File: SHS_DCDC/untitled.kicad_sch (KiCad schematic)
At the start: 32 parts, among them J1 PJ-059A, Q1 BSS84, Q14 PMV100XPEAR, Q15 2N7002-dk_Transistors-FETs-MO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, Q16 PMV100XPEAR, Q22 2N7002-dk_Transistors-FETs-MO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, Q23 2N7002-dk_Transistors-FETs-MO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, U1 RT8299-WDFN10L

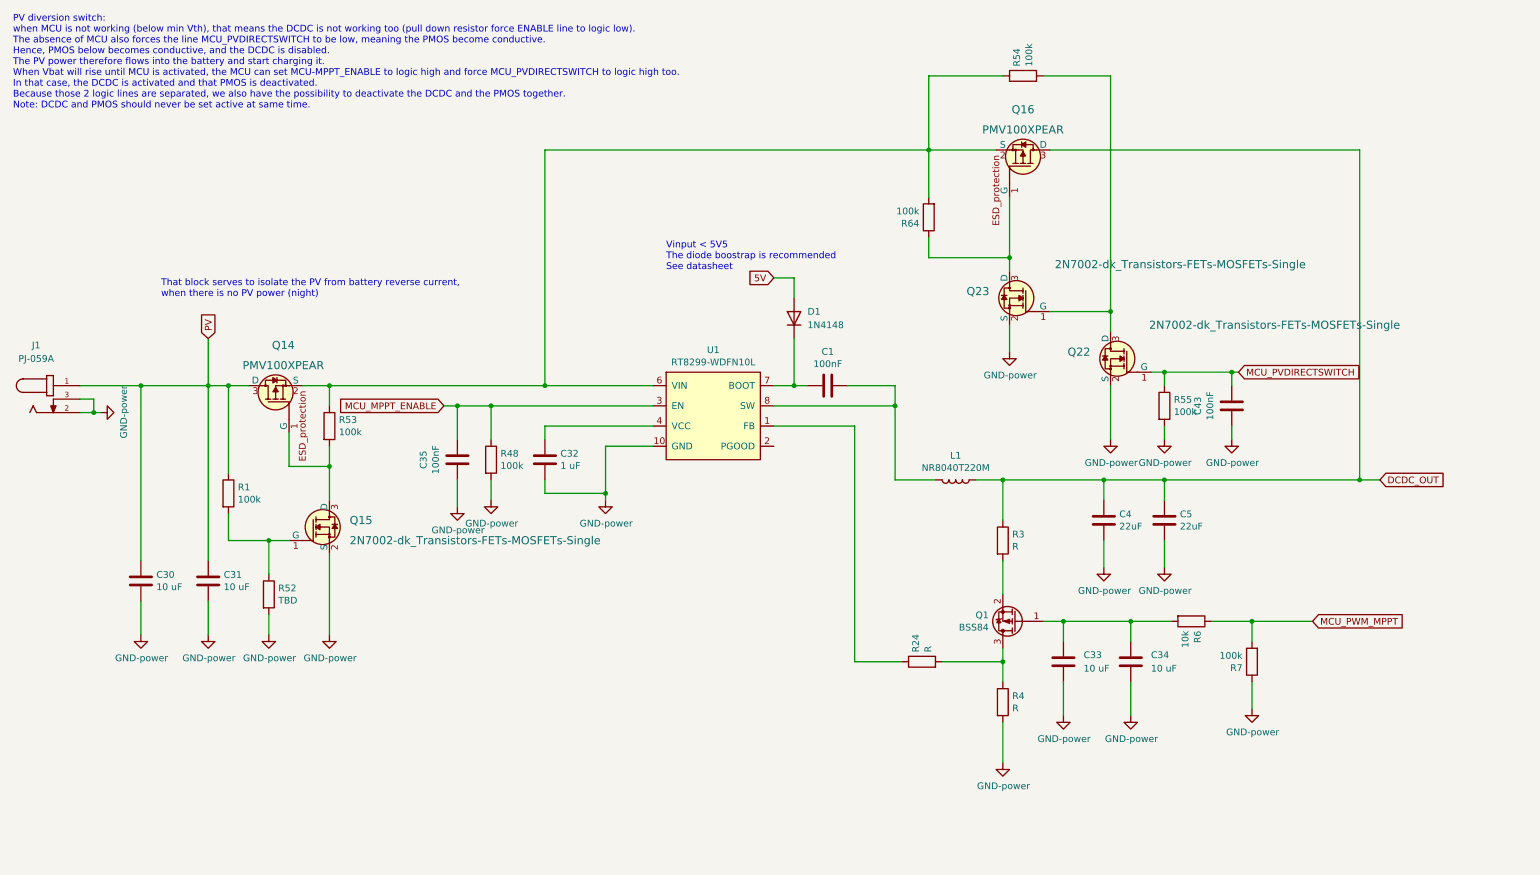
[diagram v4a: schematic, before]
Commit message: Commit before reannotation
Plan to test the reannotation feature.
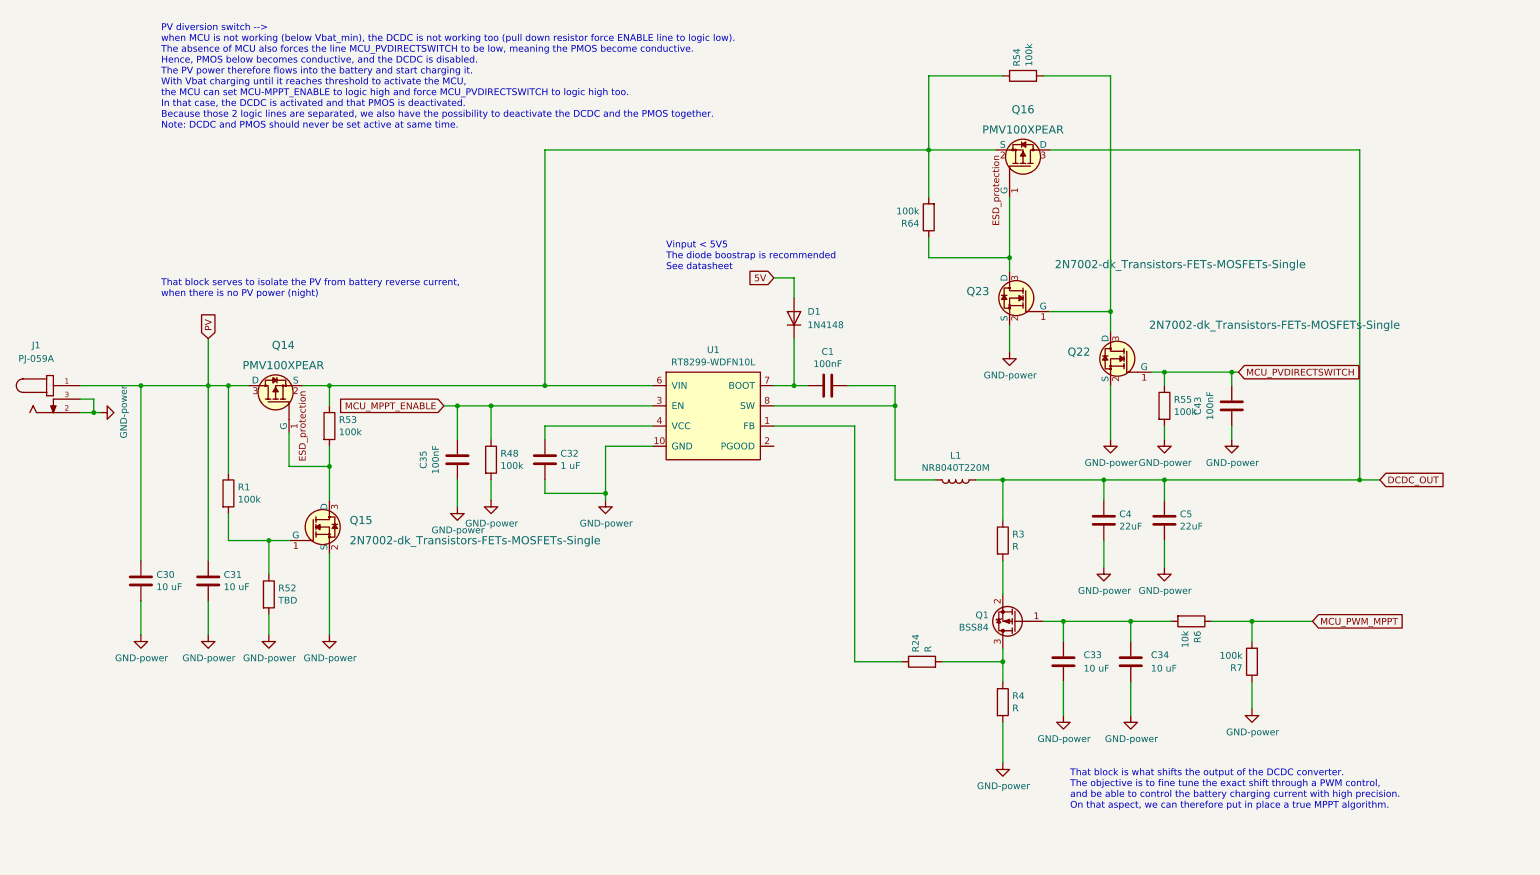
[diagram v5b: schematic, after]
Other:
- note added: "PV diversion switch --> when MCU is not working (below Vbat_min), the DCDC is not working too (pull down resistor force ENABLE line to logic low). The absence of MCU also forces the line MCU_PVDIRECTSWITCH to be low, meaning the PMOS become conductive. Hence, PMOS below becomes conductive, and the DCDC is disabled. The PV power therefore flows into the battery and start charging it. With Vbat cha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"
- note added: "That block is what shifts the output of the DCDC converter. The objective is to fine tune the exact shift through a PWM control, and be able to control the battery charging current with high precision. On that aspect, we can therefore put in place a true MPPT algorithm."
- note removed: "PV diversion switch: when MCU is not working (below min Vth), that means the DCDC is not working too (pull down resistor force ENABLE line to logic low). The absence of MCU also forces the line MCU_PVDIRECTSWITCH to be low, meaning the PMOS become conductive. Hence, PMOS below becomes conductive, and the DCDC is disabled. The PV power therefore flows into the battery and start charging it. When V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"
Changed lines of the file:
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@@
     (stroke (width 0) (type default) (color 0 0 0 0))
   )
-  (text "PV diversion switch:\nwhen MCU is not working (below min Vth), that means the DCDC is not working too (pull down resistor force ENABLE line to logic low).\nThe absence of MCU also forces the line MCU_PVDIRECTSWITCH to be low, meaning the PMOS become conductive.\nHence, PMOS below becomes conductive, and the DCDC is disabled.\nThe PV power therefore flows into the battery and start charging it.\nWhen Vbat will rise until MCU is activated, the MCU can set MCU-MPPT_ENABLE to logic high and force MCU_PVDIRECTSWITCH to logic high too.\nIn that case, the DCDC is activated and that PMOS is deactivated. \nBecause those 2 logic lines are separated, we also have the possibility to deactivate the DCDC and the PMOS together. \nNote: DCDC and PMOS should never be set active at same time."
-    (at 13.97 31.75 0)
+  (text "That block is what shifts the output of the DCDC converter.\nThe objective is to fine tune the exact shift through a PWM control,\nand be able to control the battery charging current with high precision.\nOn that aspect, we can therefore put in place a true MPPT algorithm."
+    (at 213.36 163.83 0)
     (effects (font (size 1.27 1.27)) (justify left bottom))
   )
+  (text "PV diversion switch -->\nwhen MCU is not working (below Vbat_min), the DCDC is not working too (pull down resistor force ENABLE line to logic low).\nThe absence of MCU also forces the line MCU_PVDIRECTSWITCH to be low, meaning the PMOS become conductive.\nHence, PMOS below becomes conductive, and the DCDC is disabled.\nThe PV power therefore flows into the battery and start charging it.\nWith Vbat charging until it reaches threshold to activate the MCU, \nthe MCU can set MCU-MPPT_ENABLE to logic high and force MCU_PVDIRECTSWITCH to logic high too.\nIn that case, the DCDC is activated and that PMOS is deactivated. \nBecause those 2 logic lines are separated, we also have the possibility to deactivate the DCDC and the PMOS together. \nNote: DCDC and PMOS should never be set active at same time."
+    (at 41.91 35.56 0)
+    (effects (font (size 1.27 1.27)) (justify left bottom))
+  )

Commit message: Testpoints
All the tests points have been placed
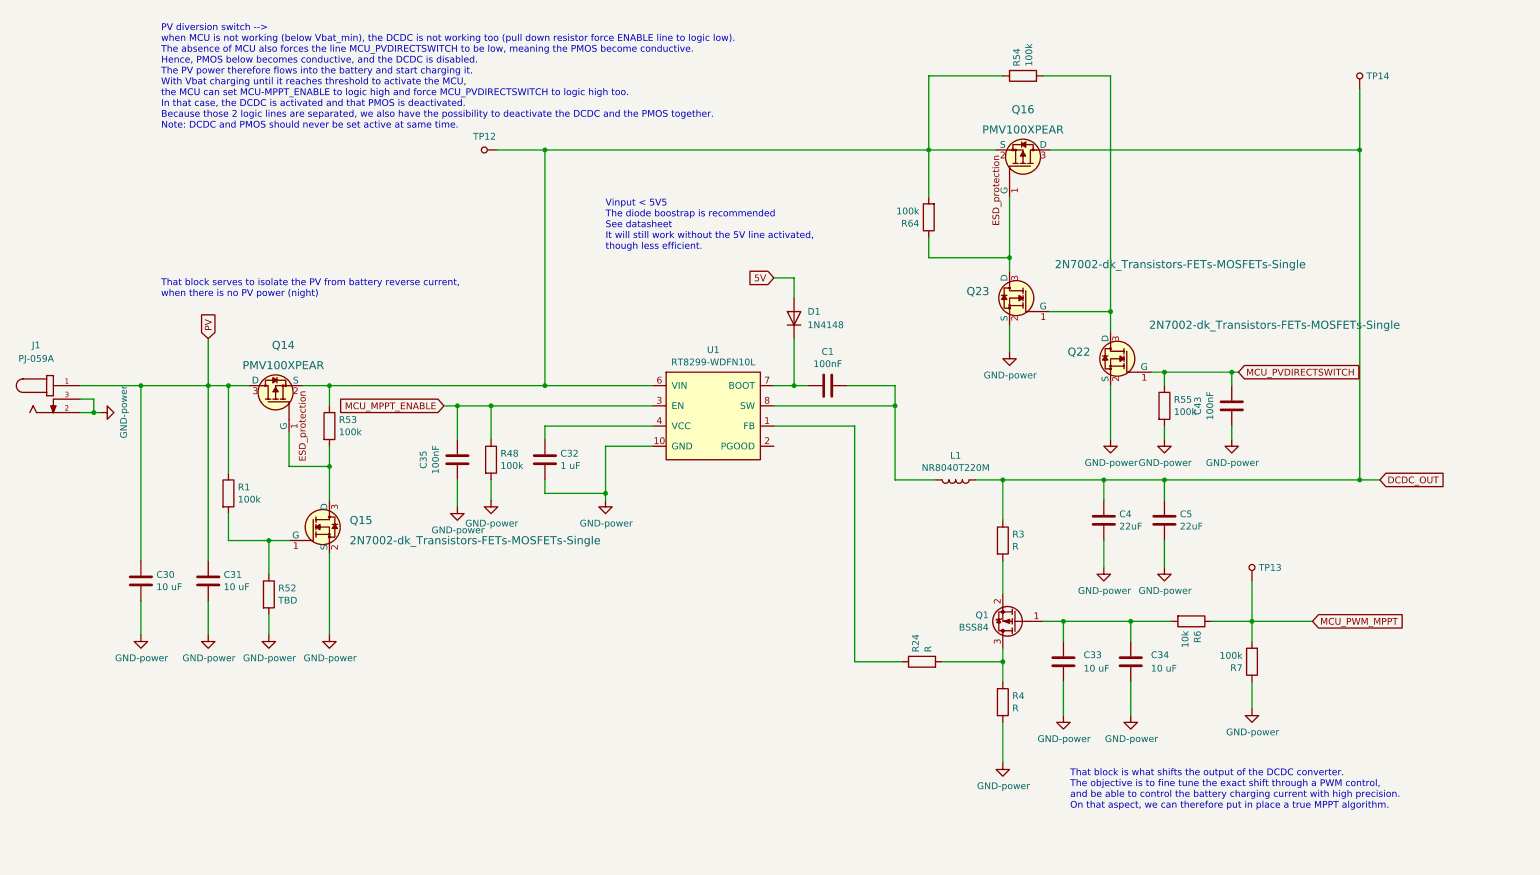
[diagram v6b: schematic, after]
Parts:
- added TP12, TP13, TP14: 5029, digikey-footprints:PC_Test_Point_Mini_3.8x2.03mm, symbol dk_Test-Points:5029
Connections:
- net DCDC_OUT: now also TP14.1
- net MCU_PWM_MPPT: now also TP13.1
- net at Q14.2 (S), Q16.2 (S), R53.1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: now also TP12.1
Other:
- note added: "Vinput < 5V5 The diode boostrap is recommended See datasheet It will still work without the 5V line activated, though less efficient."
- note removed: "Vinput < 5V5 The diode boostrap is recommended See datasheet"
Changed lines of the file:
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@@
 (kicad_sch (version 20211123) (generator eeschema)
   (paper "A4")
+  (junction (at 267.97 39.37) (diameter 0) (color 0 0 0 0)
+  )
   (junction (at 125.73 104.14) (diameter 0) (color 0 0 0 0)
   )
@@
   (junction (at 200.66 101.6) (diameter 0) (color 0 0 0 0)
   )
+  (junction (at 114.3 39.37) (diameter 0) (color 0 0 0 0)
+  )
   (junction (at 73.66 83.82) (diameter 0) (color 0 0 0 0)
   )
@@
     (stroke (width 0) (type default) (color 0 0 0 0))
   )
+  (wire (pts (xy 267.97 27.94) (xy 267.97 39.37))
+    (stroke (width 0) (type default) (color 0 0 0 0))
+  )
   (wire (pts (xy 243.84 81.28) (xy 243.84 83.82))
     (stroke (width 0) (type default) (color 0 0 0 0))
@@
     (stroke (width 0) (type default) (color 0 0 0 0))
   )
+  (wire (pts (xy 105.41 39.37) (xy 114.3 39.37))
+    (stroke (width 0) (type default) (color 0 0 0 0))
+  )
   (wire (pts (xy 38.1 116.84) (xy 38.1 83.82))
     (stroke (width 0) (type default) (color 0 0 0 0))
@@
   )
   (wire (pts (xy 201.93 72.39) (xy 201.93 77.47))
+    (stroke (width 0) (type default) (color 0 0 0 0))
+  )
+  (wire (pts (xy 247.65 120.65) (xy 247.65 128.27))
     (stroke (width 0) (type default) (color 0 0 0 0))
   )
@@
     (effects (font (size 1.27 1.27)) (justify left bottom))
   )
-  (text "Vinput < 5V5\nThe diode boostrap is recommended\nSee datasheet"
-    (at 137.16 62.23 0)
+  (text "Vinput < 5V5\nThe diode boostrap is recommended\nSee datasheet\nIt will still work without the 5V line activated,\nthough less efficient."
+    (at 125.73 58.42 0)
     (effects (font (size 1.27 1.27)) (justify left bottom))
   )
@@
     (pin "2")
   )
+  (symbol (lib_id "dk_Test-Points:5029") (at 247.65 118.11 180) (unit 1)
+    (in_bom yes) (on_board yes) (fields_autoplaced)
+    (property "Reference" "TP13" (id 0) (at 248.92 118.148 0)
+      (effects (font (size 1.27 1.27)) (justify right))
+    )
+    (property "Value" "5029" (id 1) (at 247.65 115.57 0)
+      (effects (font (size 1.27 1.27)) hide)
+    )
+    (property "Footprint" "digikey-footprints:PC_Test_Point_Mini_3.8x2.03mm" (id 2) (at 242.57 123.19 0)
+      (effects (font (size 1.524 1.524)) (justify left) hide)
+    )
+    (property "Datasheet" "http://www.keyelco.com/product-pdf.cfm?p=1358" (id 3) (at 242.57 125.73 0)
+      (effects (font (size 1.524 1.524)) (justify left) hide)
+    )
+    (property "Digi-Key_PN" "36-5029CT-ND" (id 4) (at 242.57 128.27 0)
+      (effects (font (size 1.524 1.524)) (justify left) hide)
+    )
+    (property "MPN" "5029" (id 5) (at 242.57 130.81 0)
+      (effects (font (size 1.524 1.524)) (justify left) hide)
+    )
+    (property "Category" "Test and Measurement" (id 6) (at 242.57 133.35 0)
+      (effects (font (size 1.524 1.524)) (justify left) hide)
+    )
+    (property "Family" "Test Points" (id 7) (at 242.57 135.89 0)
+      (effects (font (size 1.524 1.524)) (justify left) hide)
+    )
+    (property "DK_Datasheet_Link" "http://www.keyelco.com/product-pdf.cfm?p=1358" (id 8) (at 242.57 138.43 0)
+      (effects (font (size 1.524 1.524)) (justify left) hide)
+    )
+    (property "DK_Detail_Page" "/product-detail/en/keystone-electronics/5029/36-5029CT-ND/5980631" (id 9) (at 242.57 140.97 0)
+      (effects (font (size 1.524 1.524)) (justify left) hide)
+    )
+    (property "Description" "PC TEST POINT MINIATURE" (id 10) (at 242.57 143.51 0)
+      (effects (font (size 1.524 1.524)) (justify left) hide)
+    )
+    (property "Manufacturer" "Keystone Electronics" (id 11) (at 242.57 146.05 0)
+      (effects (font (size 1.524 1.524)) (justify left) hide)
+    )
+    (property "Status" "Active" (id 12) (at 242.57 148.59 0)
+      (effects (font (size 1.524 1.524)) (justify left) hide)
+    )
+    (pin "1")
+  )
   (symbol (lib_id "SHS_DCDC:R-Device") (at 186.69 52.07 180) (unit 1)
     (in_bom yes) (on_board yes)
@@
     (pin "3")
   )
+  (symbol (lib_id "dk_Test-Points:5029") (at 267.97 25.4 180) (unit 1)
+    (in_bom yes) (on_board yes) (fields_autoplaced)
+    (property "Reference" "TP14" (id 0) (at 269.24 25.438 0)
+      (effects (font (size 1.27 1.27)) (justify right))
+    )
+    (property "Value" "5029" (id 1) (at 267.97 22.86 0)
+      (effects (font (size 1.27 1.27)) hide)
+    )
+    (property "Footprint" "digikey-footprints:PC_Test_Point_Mini_3.8x2.03mm" (id 2) (at 262.89 30.48 0)
+      (effects (font (size 1.524 1.524)) (justify left) hide)
+    )
+    (property "Datasheet" "http://www.keyelco.com/product-pdf.cfm?p=1358" (id 3) (at 262.89 33.02 0)
+      (effects (font (size 1.524 1.524)) (justify left) hide)
+    )
+    (property "Digi-Key_PN" "36-5029CT-ND" (id 4) (at 262.89 35.56 0)
+      (effects (font (size 1.524 1.524)) (justify left) hide)
+    )
+    (property "MPN" "5029" (id 5) (at 262.89 38.1 0)
+      (effects (font (size 1.524 1.524)) (justify left) hide)
+    )
+    (property "Category" "Test and Measurement" (id 6) (at 262.89 40.64 0)
+      (effects (font (size 1.524 1.524)) (justify left) hide)
+    )
+    (property "Family" "Test Points" (id 7) (at 262.89 43.18 0)
+      (effects (font (size 1.524 1.524)) (justify left) hide)
+    )
+    (property "DK_Datasheet_Link" "http://www.keyelco.com/product-pdf.cfm?p=1358" (id 8) (at 262.89 45.72 0)
+      (effects (font (size 1.524 1.524)) (justify left) hide)
+    )
+    (property "DK_Detail_Page" "/product-detail/en/keystone-electronics/5029/36-5029CT-ND/5980631" (id 9) (at 262.89 48.26 0)
+      (effects (font (size 1.524 1.524)) (justify left) hide)
+    )
+    (property "Description" "PC TEST POINT MINIATURE" (id 10) (at 262.89 50.8 0)
+      (effects (font (size 1.524 1.524)) (justify left) hide)
+    )
+    (property "Manufacturer" "Keystone Electronics" (id 11) (at 262.89 53.34 0)
+      (effects (font (size 1.524 1.524)) (justify left) hide)
+    )
+    (property "Status" "Active" (id 12) (at 262.89 55.88 0)
+      (effects (font (size 1.524 1.524)) (justify left) hide)
+    )
+    (pin "1")
+  )
   (symbol (lib_id "SHS_DCDC:PMV100XPEAR") (at 63.5 83.82 90) (unit 1)
     (in_bom yes) (on_board yes)
@@
     (pin "2")
   )
+  (symbol (lib_id "dk_Test-Points:5029") (at 102.87 39.37 270) (unit 1)
+    (in_bom yes) (on_board yes) (fields_autoplaced)
+    (property "Reference" "TP12" (id 0) (at 102.9081 36.83 90))
+    (property "Value" "5029" (id 1) (at 100.33 39.37 0)
+      (effects (font (size 1.27 1.27)) hide)
+    )
+    (property "Footprint" "digikey-footprints:PC_Test_Point_Mini_3.8x2.03mm" (id 2) (at 107.95 44.45 0)
+      (effects (font (size 1.524 1.524)) (justify left) hide)
+    )
+    (property "Datasheet" "http://www.keyelco.com/product-pdf.cfm?p=1358" (id 3) (at 110.49 44.45 0)
+      (effects (font (size 1.524 1.524)) (justify left) hide)
+    )
+    (property "Digi-Key_PN" "36-5029CT-ND" (id 4) (at 113.03 44.45 0)
+      (effects (font (size 1.524 1.524)) (justify left) hide)
+    )
+    (property "MPN" "5029" (id 5) (at 115.57 44.45 0)
+      (effects (font (size 1.524 1.524)) (justify left) hide)
+    )
+    (property "Category" "Test and Measurement" (id 6) (at 118.11 44.45 0)
+      (effects (font (size 1.524 1.524)) (justify left) hide)
+    )
+    (property "Family" "Test Points" (id 7) (at 120.65 44.45 0)
+      (effects (font (size 1.524 1.524)) (justify left) hide)
+    )
+    (property "DK_Datasheet_Link" "http://www.keyelco.com/product-pdf.cfm?p=1358" (id 8) (at 123.19 44.45 0)
+      (effects (font (size 1.524 1.524)) (justify left) hide)
+    )
+    (property "DK_Detail_Page" "/product-detail/en/keystone-electronics/5029/36-5029CT-ND/5980631" (id 9) (at 125.73 44.45 0)
+      (effects (font (size 1.524 1.524)) (justify left) hide)
+    )
+    (property "Description" "PC TEST POINT MINIATURE" (id 10) (at 128.27 44.45 0)
+      (effects (font (size 1.524 1.524)) (justify left) hide)
+    )
+    (property "Manufacturer" "Keystone Electronics" (id 11) (at 130.81 44.45 0)
+      (effects (font (size 1.524 1.524)) (justify left) hide)
+    )
+    (property "Status" "Active" (id 12) (at 133.35 44.45 0)
+      (effects (font (size 1.524 1.524)) (justify left) hide)
+    )
+    (pin "1")
+  )
   (symbol (lib_id "SHS_DCDC:GND-power") (at 224.79 146.05 0) (unit 1)
